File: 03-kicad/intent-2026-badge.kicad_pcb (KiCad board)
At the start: 2 copper layers, 56 x 124 mm, 97 parts, among them J1 TYPE-C-31-M-12, J2 HACK HEADER, J3 BATT 3xAAA, J4 PJ-320D, J5 SAO1 IR, J6 SAO2 AUDIO, J7 SAO3 SPK, P1 IR MODULE, P2 AUDIO MODULE, P3 SPK MODULE, Q1 HL3401, Q2 S8050, SW1 BOOTSEL, SW2 A, SW3 B, SW4 C, SW5 MSK12C02, SW6 RESET, U1 RP2040, U2 W25Q16JVSNIQ, U3 AP2112K-3.3TRG1, U4 USBLC6-2SC6, U5 IRM-H638T/TR2, U6 SN74LV1T34DBVR, Y1 12MHz ABM8-272-T3

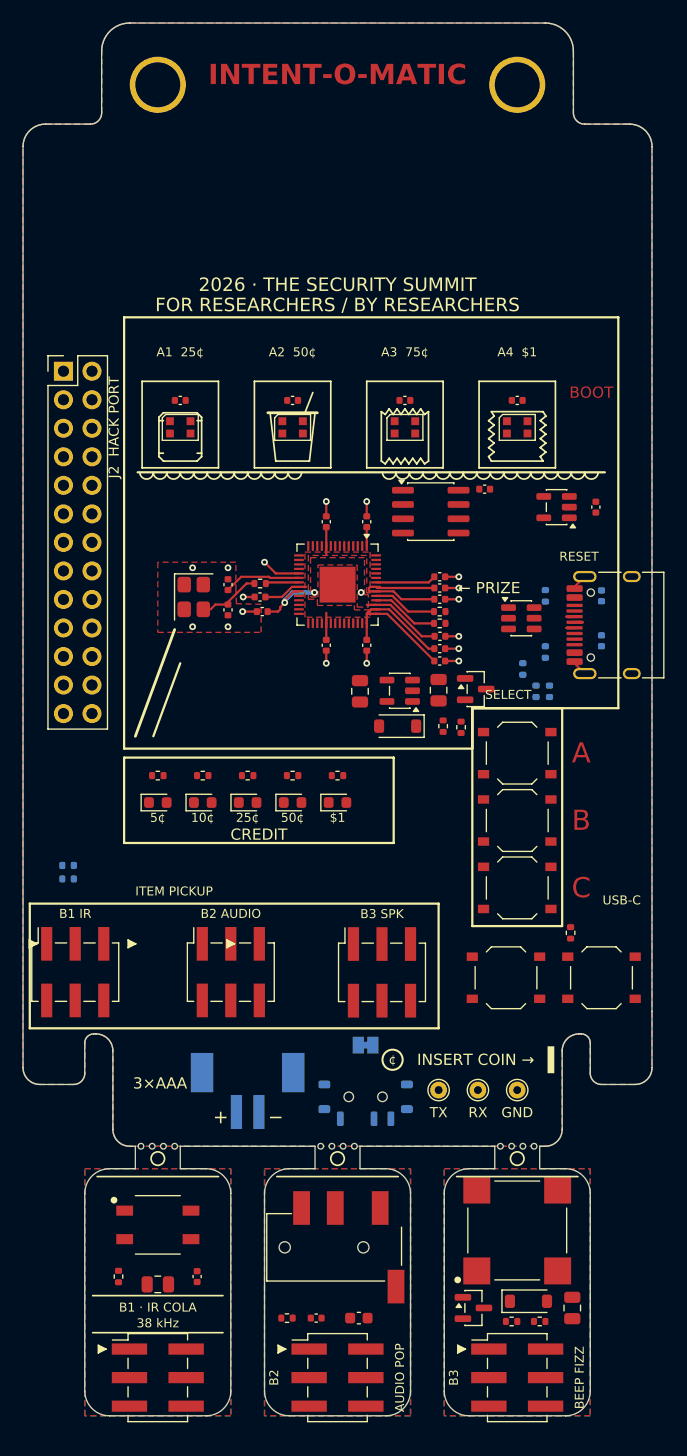
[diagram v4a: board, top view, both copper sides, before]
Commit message: Board: more hand routing (26 unconnected left per DRC)
Co-Authored-By: Claude Opus 5.5 (1M context) <noreply@anthropic.com>
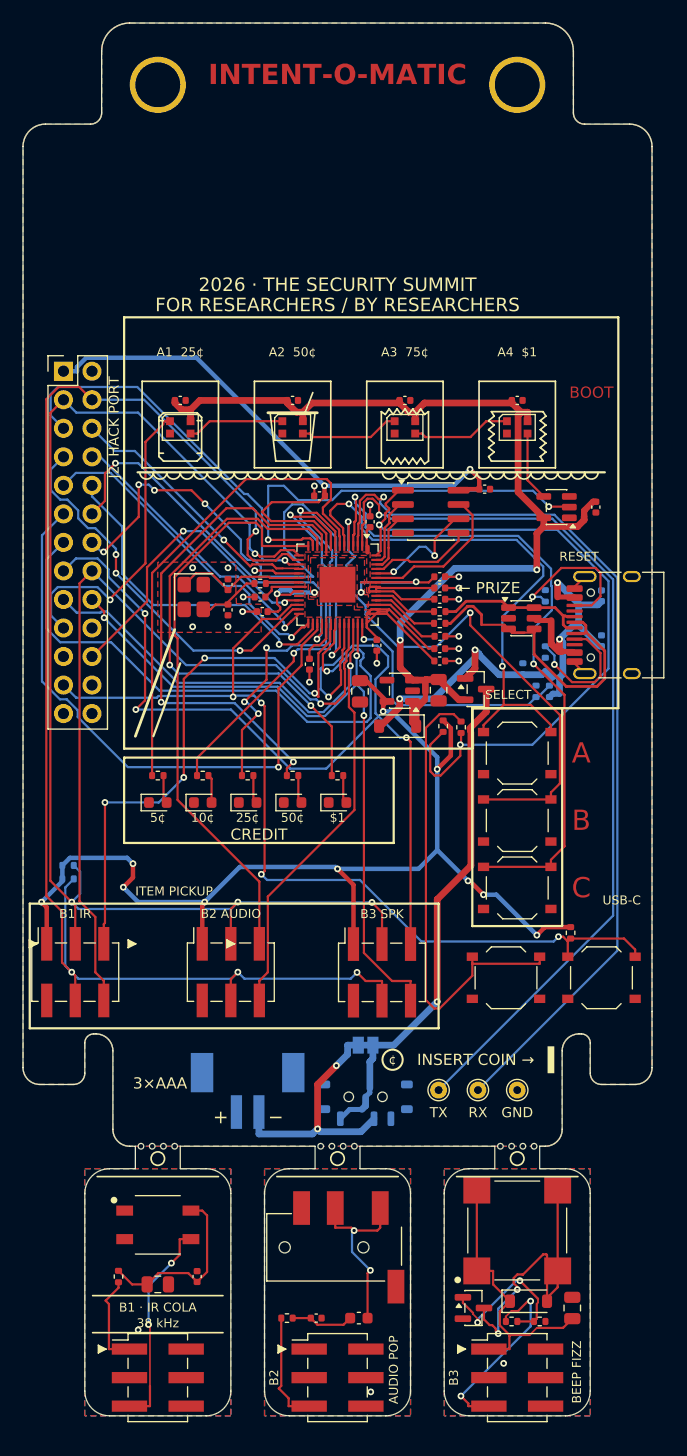
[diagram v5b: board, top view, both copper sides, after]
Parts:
- moved C2 2.38 mm to (126.4, 92.1), turned to 180 degrees
- moved C4 2.25 mm to (125.5, 107.1)
- moved C5 0.90 mm to (131.5, 105.4)
- moved C1 0.30 mm to (130.9, 94.4)
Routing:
- net +3V3: track 40.5 -> 204.2 mm, vias 0 -> 12
- net SAO_SCL: track 0.00 -> 130.0 mm, vias 0 -> 4
- net SAO_SDA: track 0.00 -> 117.6 mm, vias 0 -> 4
- net VSYS: track 0.00 -> 91.4 mm, vias 0 -> 2
- net SPK_PWM: track 0.00 -> 89.7 mm, vias 0 -> 4
- net RUN: track 0.00 -> 84.4 mm, vias 0 -> 4
- net UART0_RX: track 0.00 -> 82.0 mm, vias 0 -> 1
- net UART0_TX: track 0.00 -> 81.8 mm, vias 0 -> 1
- net SAO1_GPIO2: track 0.00 -> 73.9 mm, vias 0 -> 1
- net SAO2_GPIO2: track 0.00 -> 69.9 mm, vias 0 -> 1
- net SAO3_GPIO2: track 0.00 -> 65.9 mm, vias 0 -> 3
- net QSPI_SS: track 0.00 -> 63.2 mm, vias 0 -> 2
- net BTN_C: track 0.00 -> 60.7 mm, vias 0 -> 2
- net GPIO23: track 0.00 -> 56.2 mm, vias 0 -> 1
- net GPIO24: track 0.00 -> 55.9 mm, vias 0 -> 5
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
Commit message: Board: routing complete (DRC 0 errors, 0 unconnected), fab outputs regenerated
Benny's hand routing plus the scripted GND fixes (U1 exposed-pad vias,
stitching vias, IR module pour joint). Gerbers, JLC BOM/CPL, DRC/ERC reports
and renders regenerated from this board. Review notes in BUILD-NOTES item 17.

Co-Authored-By: Claude Opus 5.5 (1M context) <noreply@anthropic.com>
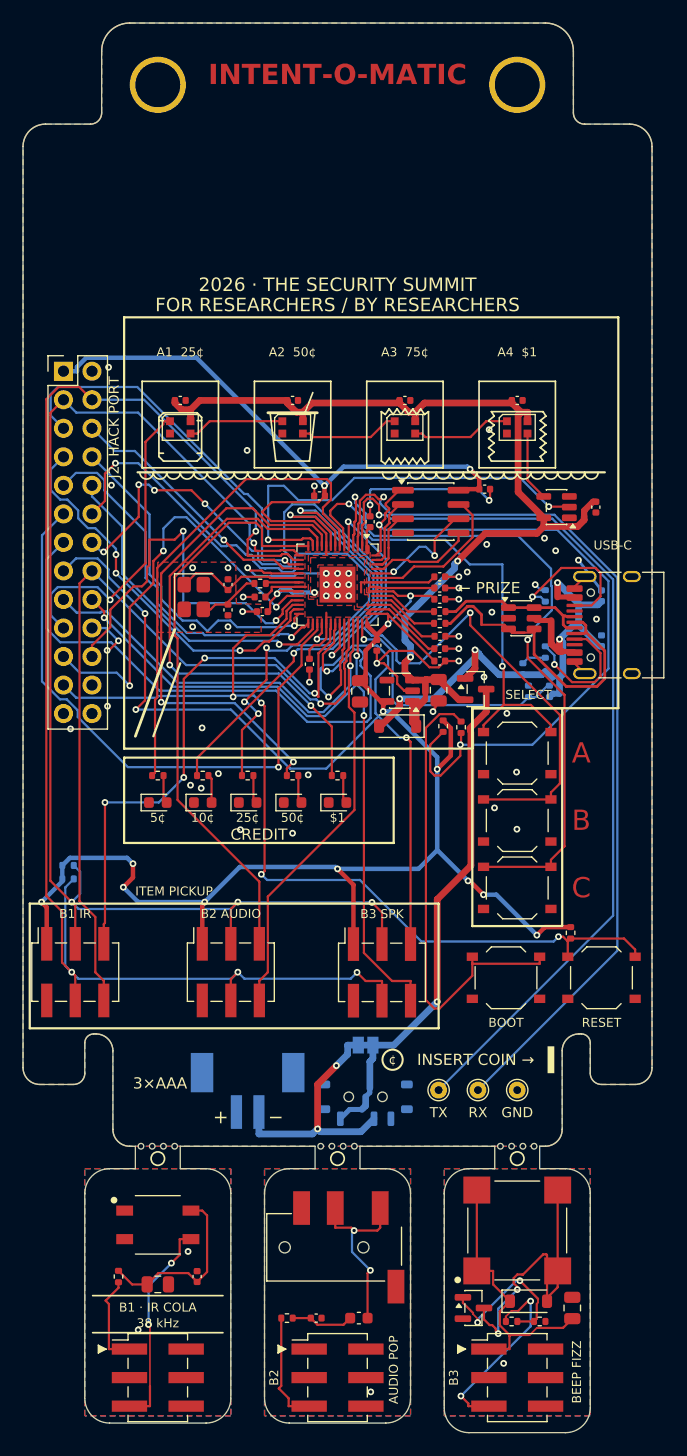
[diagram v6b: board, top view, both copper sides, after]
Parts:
- moved R16 0.67 mm to (145.0, 109.5)
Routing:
- net GND: track 20.7 -> 66.1 mm, vias 17 -> 56
- net SWCLK: track 0.00 -> 38.5 mm, vias 0 -> 3
- net GPIO21: track 34.6 -> 44.6 mm
- net +3V3: track 204.2 -> 212.5 mm, vias 12 -> 14
- net SWDIO: track 27.5 -> 34.8 mm
- net +1V1: track 28.2 -> 22.6 mm, vias 4 -> 2
- net BTN_A: track 48.4 -> 43.4 mm
- net LED_R3: track 37.4 -> 42.4 mm
- net GPIO17: track 25.5 -> 30.2 mm
- net LED_R2: track 36.6 -> 40.8 mm
- net GPIO18: track 29.3 -> 32.7 mm
- net BTN_B: track 50.2 -> 53.3 mm
- net VSYS: track 91.4 -> 89.7 mm
- net GPIO24: track 55.9 -> 55.0 mm
- net RGB_CTRL: track 37.7 -> 38.6 mm
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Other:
- board size 56 x 124 mm -> 56 x 125.5 mm

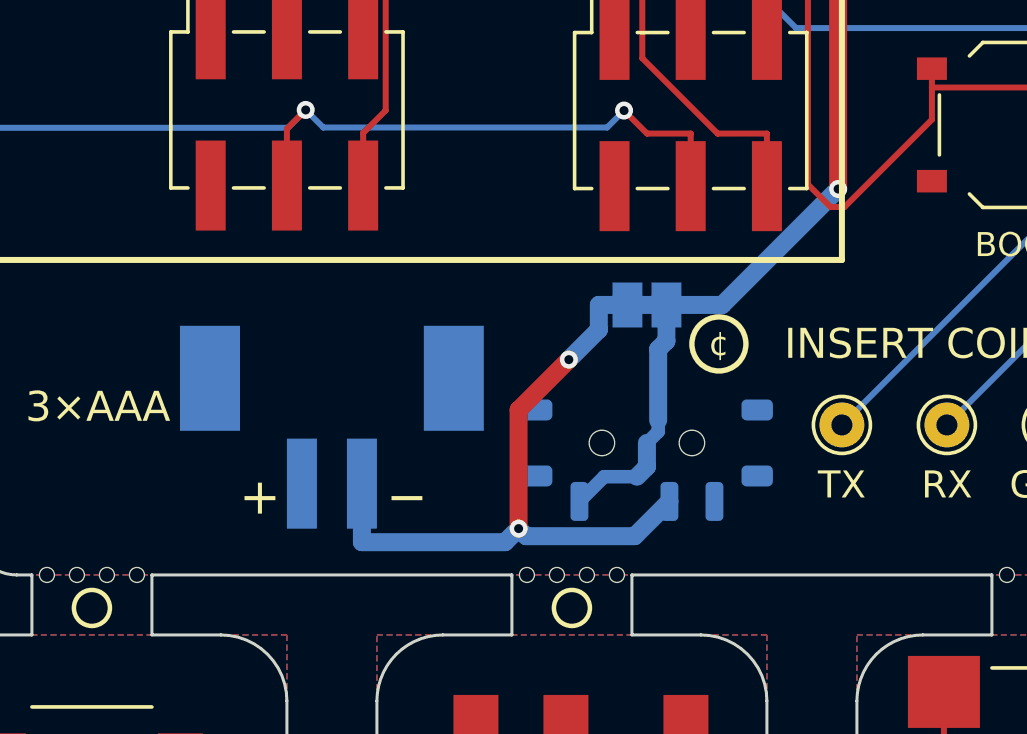
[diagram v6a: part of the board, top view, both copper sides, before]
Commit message: J3 -> JST B2B-PH-SM4-TB (C160352), drop SW5/JP1
- J3 battery-box plug is now a genuine JST PH 2-pin SMD vertical
  (C160352) on the stock KiCad footprint; pin 1 = BAT_IN, pin 2 = GND.
- SW5 and JP1 removed (Benny's schematic edit): J3 feeds Q1 directly.
  design.py, gen_sch.py, placement.py, silk.py synced to the KiCad
  schematic (check_sch: 313 pins, 78 nets, 0 problems).
- PCB: J3 footprint swapped in place, SW5/JP1 removed, JP1 pads bridged,
  SW5 stubs deleted. DRC 0 errors, 0 unconnected.
- 04-fab regenerated; BOM deltas (EN + HE), BUILD-NOTES item 19, CLAUDE.md.

Co-Authored-By: Claude Opus 5.5 (1M context) <noreply@anthropic.com>
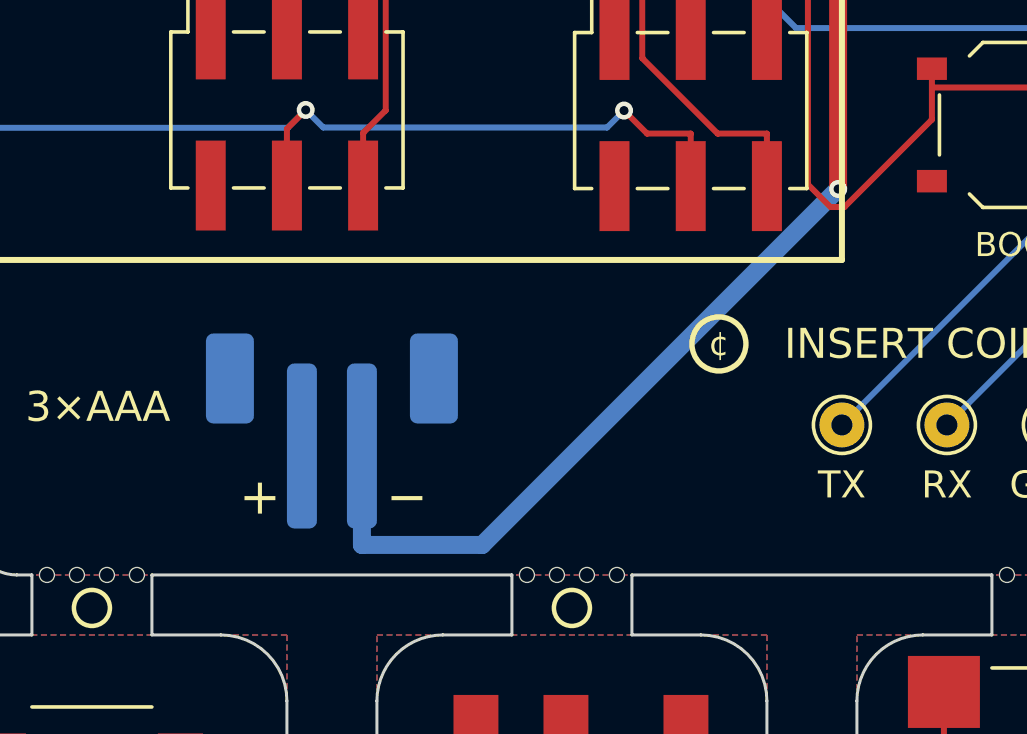
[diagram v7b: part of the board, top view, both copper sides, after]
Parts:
- removed JP1: SW5 bypass, Jumper:SolderJumper-2_P1.3mm_Bridged_Pad1.0x1.5mm
- removed SW5: MSK12C02, Button_Switch_SMD:SW_SPDT_Shouhan_MSK12C02
- J3: footprint intent:JST_PH_2P_SMD_Vertical_C722761 -> Connector_JST:JST_PH_B2B-PH-SM4-TB_1x02-1MP_P2.00mm_Vertical
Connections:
- Q1 pad 3: BAT_SW -> BAT_IN
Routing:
- net BAT_SW: track 45.4 -> 0.00 mm, vias 1 -> 0
- net BAT_IN: track 22.5 -> 53.8 mm, vias 2 -> 1

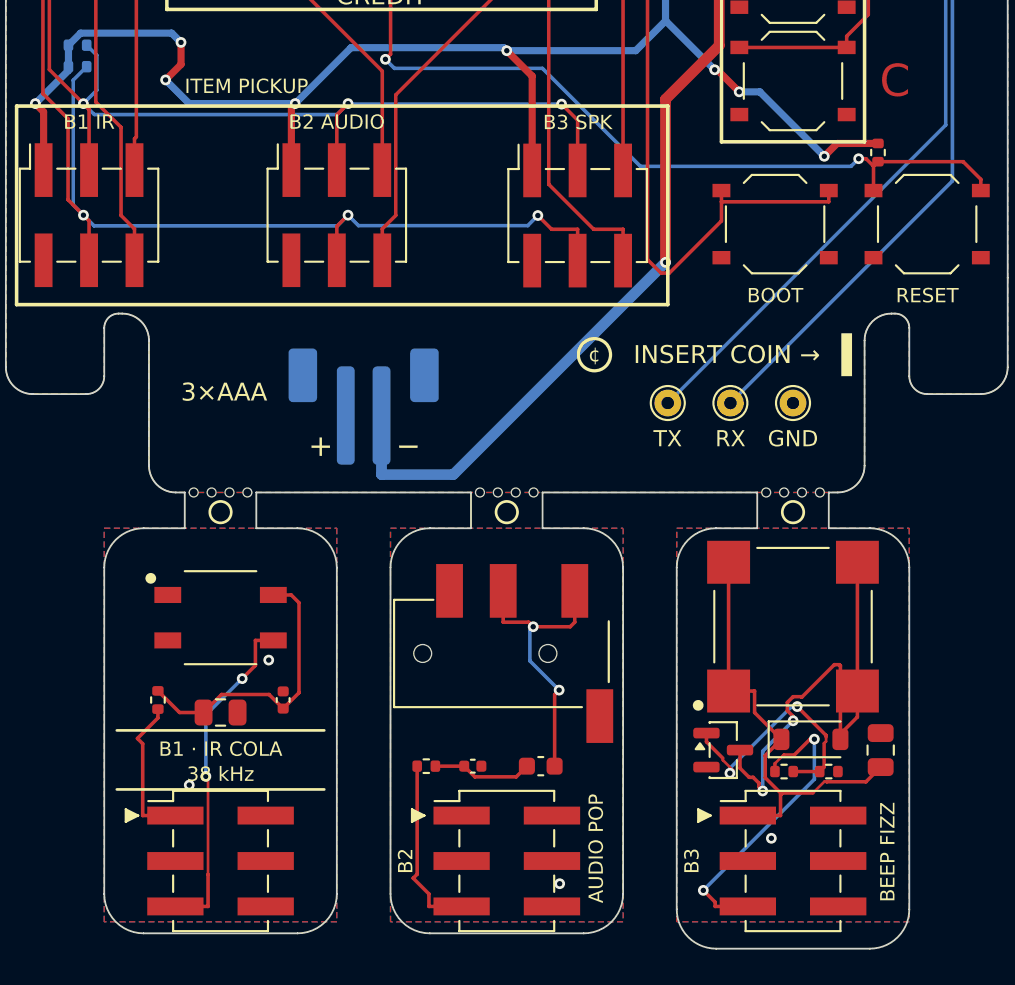
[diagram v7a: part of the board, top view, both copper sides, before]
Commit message: IMU module replaces the audio module; module SAO headers rotated 90 deg
- B2 module: ST LSM6DS3TR-C (C967633) on the SAO I2C bus at 0x6A,
  INT1 -> GPIO11 (net IMU_INT1), INT2 -> GPIO27, 100 nF on VDD/VDDIO.
  Jack, PWM filter (J4, R17, C21, C22) removed; nets AUM_* -> IMM_*.
- Module headers P1-P3 at rot 90 like the badge sockets; speaker-can
  driver row moved to the back; module silk redrawn.
- PCB edits on the hand-routed board: only module copper re-routed;
  Benny's J3/BAT_IN edit kept. DRC 0 errors, 0 unconnected.
- 04-fab regenerated; BOM deltas EN/HE, BUILD-NOTES 20/21, GPIO map.

Co-Authored-By: Claude Opus 5.5 (1M context) <noreply@anthropic.com>
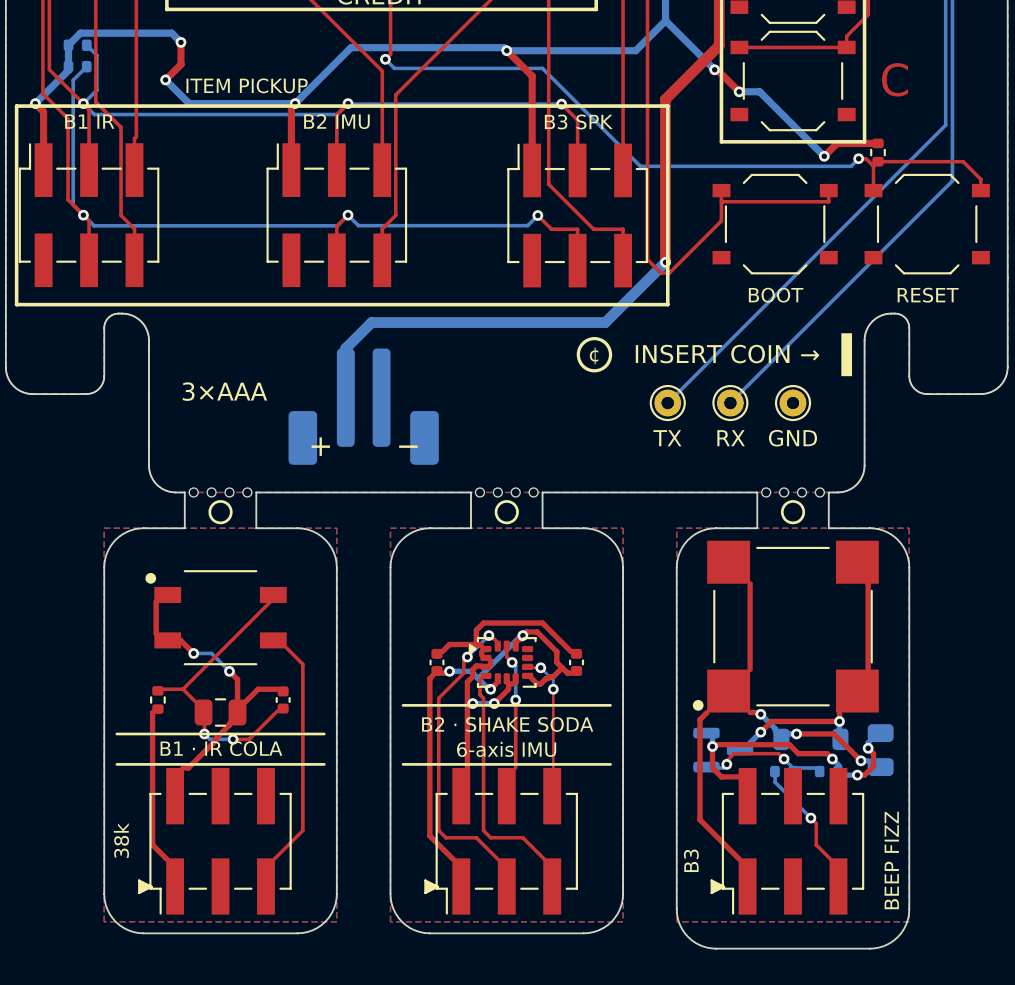
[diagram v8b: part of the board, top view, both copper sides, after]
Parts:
- removed C21: 10nF, Capacitor_SMD:C_0402_1005Metric
- removed C22: 10uF, Capacitor_SMD:C_0603_1608Metric
- removed J4: PJ-320D, intent:Jack_3.5mm_PJ-320D_SMD_C431535
- removed R17: 1k, Resistor_SMD:R_0402_1005Metric
- added C30: 100nF, Capacitor_SMD:C_0402_1005Metric, F.Cu at (124.1, 159.5)
- added C31: 100nF, Capacitor_SMD:C_0402_1005Metric, F.Cu at (131.9, 159.5)
- added U7: LSM6DS3TR-C, Package_LGA:LGA-14_3x2.5mm_P0.5mm_LayoutBorder3x4y, F.Cu at (128.0, 159.5)
- C25, D7, Q2, R20, R21: moved to B.Cu
- J6: value SAO2 AUDIO -> SAO2 IMU
- P2: value AUDIO MODULE -> IMU MODULE
- moved P1 1.10 mm to (112.0, 169.5), turned to 90 degrees
- moved P2 1.10 mm to (128.0, 169.5), turned to 90 degrees
- moved P3 1.10 mm to (144.0, 169.5), turned to 90 degrees
- turned J3 to 0 degrees
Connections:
- net AUDIO_PWM renamed IMU_INT1
- P2 pad 1: unconnected-(P2-Pin_1-Pad1) -> IMM_3V3
- P2 pad 2: AUM_GND -> IMM_GND
- P2 pad 3: unconnected-(P2-Pin_3-Pad3) -> IMM_SDA
- P2 pad 4: unconnected-(P2-Pin_4-Pad4) -> IMM_SCL
- P2 pad 5: AUM_PWM -> IMM_INT1
- P2 pad 6: unconnected-(P2-Pin_6-Pad6) -> IMM_INT2
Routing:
- net IMM_3V3: track 0.00 -> 24.8 mm, vias 0 -> 3
- net IMM_GND: track 0.00 -> 19.2 mm, vias 0 -> 2
- net IMM_SDA: track 0.00 -> 16.5 mm, vias 0 -> 2
- net AUM_OUT: track 16.4 -> 0.00 mm, vias 2 -> 0
- net SPM_COL: track 27.0 -> 11.3 mm
- net SPM_GND: track 0.00 -> 14.6 mm, vias 1 -> 4
- net IRM_GND: track 0.00 -> 14.3 mm
- net IMM_INT1: track 0.00 -> 12.7 mm
- net SPM_SIG: track 17.2 -> 5.88 mm, vias 2 -> 1
- net AUM_PWM: track 10.1 -> 0.00 mm
- net SPM_BASE: track 14.3 -> 5.84 mm
- net IMM_SCL: track 0.00 -> 6.71 mm, vias 0 -> 2
- net IMM_INT2: track 0.00 -> 6.39 mm, vias 0 -> 2
- net IRM_OUT: track 19.0 -> 12.8 mm, vias 2 -> 0
- net AUM_FILT: track 5.61 -> 0.00 mm
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- added copper zone on B.Cu, net IMM_GND
- added copper zone on F.Cu, net IMM_GND
- removed copper zone on B.Cu, net AUM_GND
- removed copper zone on F.Cu, net AUM_GND
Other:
- board text added: "38k"
- board text added: "6-axis IMU"
- board text added: "B2 IMU"
- board text added: "B2 IMU MODULE"
- board text added: "B2 · SHAKE SODA"
- board text removed: "38 kHz"
- board text removed: "AUDIO POP"
- board text removed: "B2"
- board text removed: "B2 AUDIO"
- board text removed: "B2 AUDIO MODULE"
